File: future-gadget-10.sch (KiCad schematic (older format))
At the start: 38 parts, among them J1 Conn_02x05_Odd_Even, U1 ProMicro

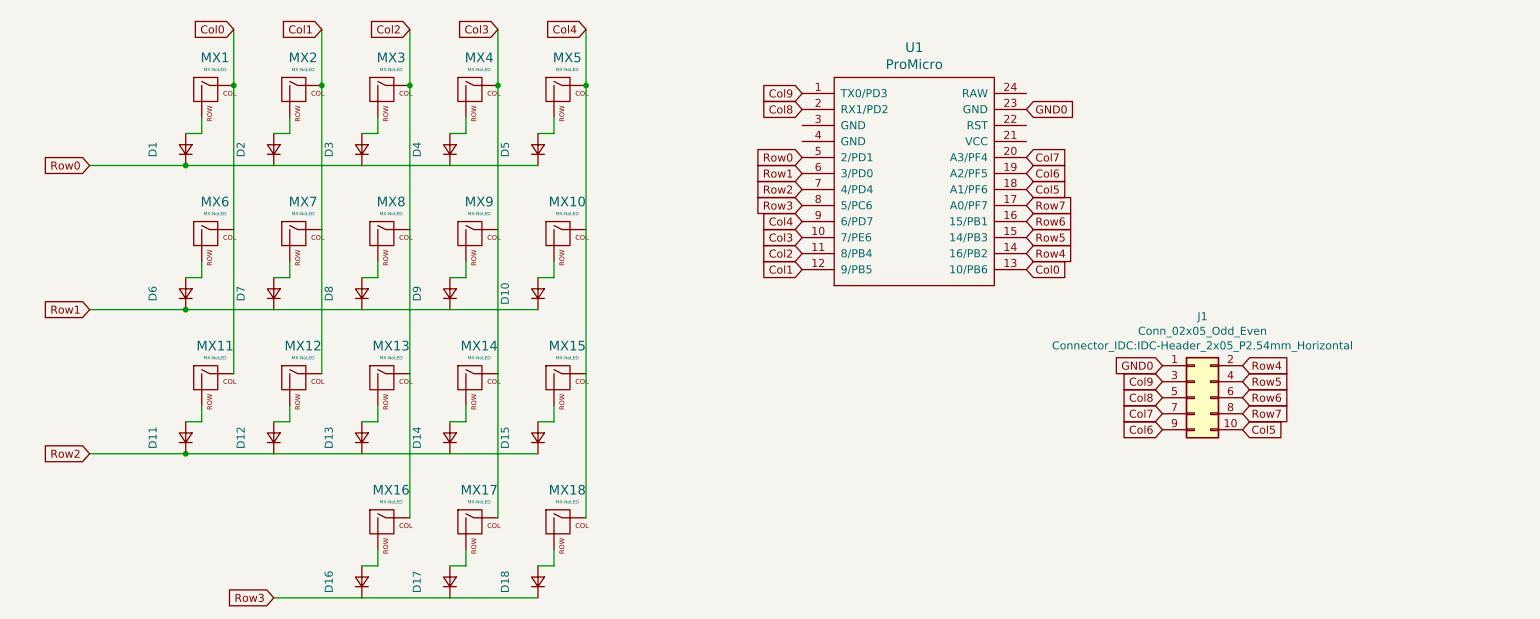
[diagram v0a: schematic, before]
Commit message: Adds right hand, and updates the connector to be vertical to avoid orientation issues.
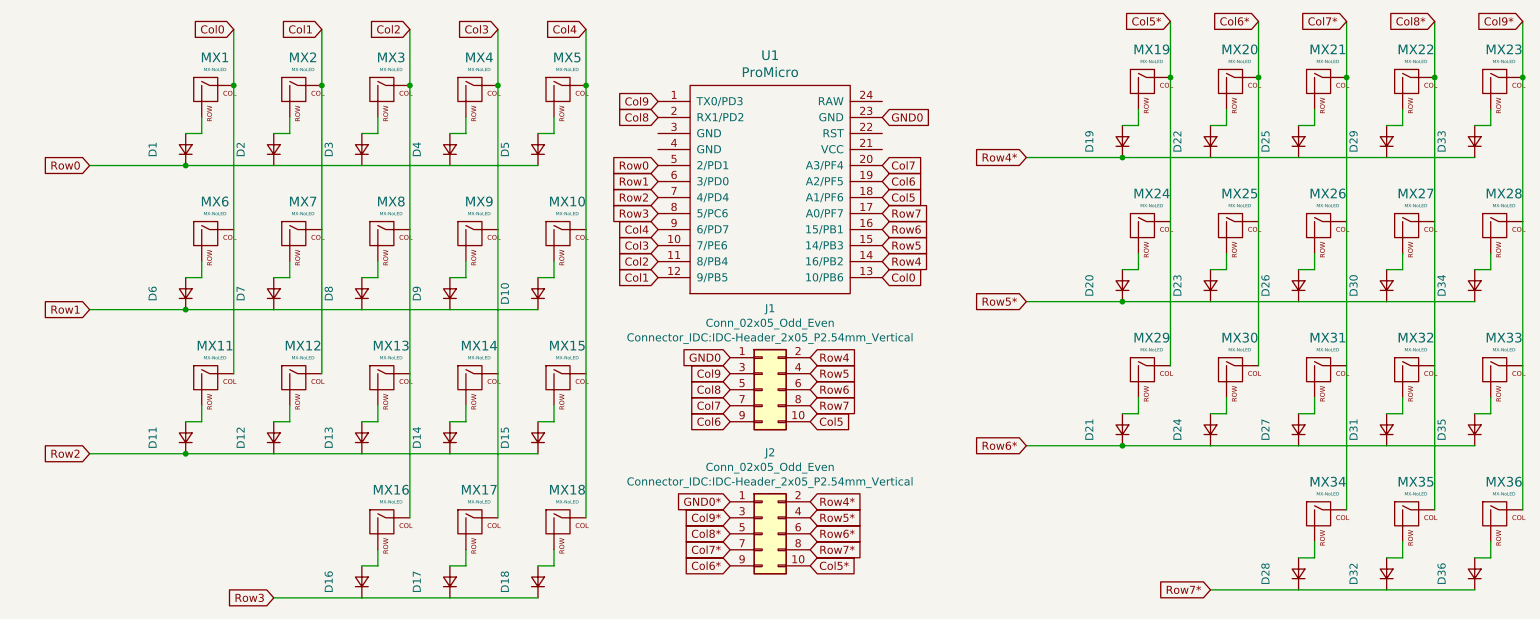
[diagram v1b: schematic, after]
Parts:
- added D19, D20, D21, D22, D23, D24, D25, D26, D27, D28, D29, D30, D31, D32, D33, D34, D35, D36: D_Small, Diode_SMD:D_SOD-123, symbol Device:D_Small
- added J2: Conn_02x05_Odd_Even, Connector_IDC:IDC-Header_2x05_P2.54mm_Vertical, symbol Connector_Generic:Conn_02x05_Odd_Even
- added MX19, MX20, MX21, MX22, MX23, MX24, MX25, MX26, MX27, MX28, MX29, MX30, MX31, MX32, MX33, MX34, MX35, MX36: MX-NoLED, MX_Only:MXOnly-1U-Hotswap, symbol MX_Alps_Hybrid:MX-NoLED
- J1: footprint Connector_IDC:IDC-Header_2x05_P2.54mm_Horizontal -> Connector_IDC:IDC-Header_2x05_P2.54mm_Vertical
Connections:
- new net: D19.2 (A), MX19.2 (ROW)
- new net: D22.2 (A), MX20.2 (ROW)
- new net: D23.2 (A), MX25.2 (ROW)
- new net: D20.2 (A), MX24.2 (ROW)
- new net: D25.2 (A), MX21.2 (ROW)
- new net: D26.2 (A), MX26.2 (ROW)
- new net: D29.2 (A), MX22.2 (ROW)
- new net: D30.2 (A), MX27.2 (ROW)
- new net: D33.2 (A), MX23.2 (ROW)
- new net: D34.2 (A), MX28.2 (ROW)
- new net: D24.2 (A), MX30.2 (ROW)
- new net: D21.2 (A), MX29.2 (ROW)
- new net: D27.2 (A), MX31.2 (ROW)
- new net: D31.2 (A), MX32.2 (ROW)
- new net: D35.2 (A), MX33.2 (ROW)
- new net: D28.2 (A), MX34.2 (ROW)
- new net: D32.2 (A), MX35.2 (ROW)
- new net: D36.2 (A), MX36.2 (ROW)
- new net Col5*: J2.10 (Pin_10), MX19.1 (COL), MX24.1 (COL), MX29.1 (COL)
- new net Col6*: J2.9 (Pin_9), MX20.1 (COL), MX25.1 (COL), MX30.1 (COL)
- new net Col7*: J2.7 (Pin_7), MX21.1 (COL), MX26.1 (COL), MX31.1 (COL), MX34.1 (COL)
- new net Col8*: J2.5 (Pin_5), MX22.1 (COL), MX27.1 (COL), MX32.1 (COL), MX35.1 (COL)
- new net Col9*: J2.3 (Pin_3), MX23.1 (COL), MX28.1 (COL), MX33.1 (COL), MX36.1 (COL)
- new net GND0*: J2.1 (Pin_1)
- new net Row4*: D19.1 (K), D22.1 (K), D25.1 (K), D29.1 (K), D33.1 (K), J2.2 (Pin_2)
- new net Row5*: D20.1 (K), D23.1 (K), D26.1 (K), D30.1 (K), D34.1 (K), J2.4 (Pin_4)
- new net Row6*: D21.1 (K), D24.1 (K), D27.1 (K), D31.1 (K), D35.1 (K), J2.6 (Pin_6)
- new net Row7*: D28.1 (K), D32.1 (K), D36.1 (K), J2.8 (Pin_8)
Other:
- moved on the sheet: J1, U1

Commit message: A little rerouting and a switch of footprints for the MX hotswaps so they render in 3D.
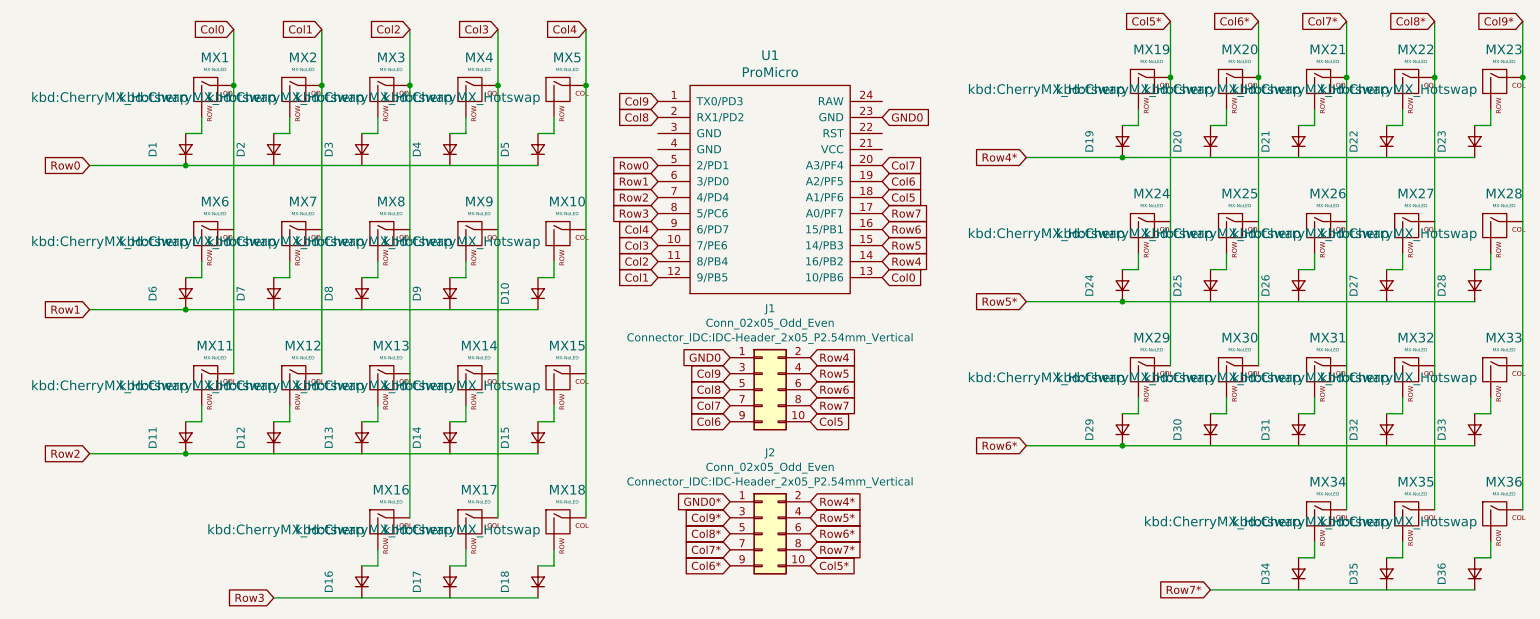
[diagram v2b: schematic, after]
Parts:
- MX1, MX10, MX11, MX12, MX13, MX14, MX15, MX16, MX17, MX18, MX19, MX2, MX20, MX21, MX22, MX23, MX24, MX25, MX26, MX27, MX28, MX29, MX3, MX30, MX31, MX32, MX33, MX34, MX35, MX36, MX4, MX5, MX6, MX7, MX8, MX9: footprint MX_Only:MXOnly-1U-Hotswap -> kbd:CherryMX_Hotswap
- renumbered D22 to D20, D25 to D21, D29 to D22, D33 to D23, D20 to D24, D23 to D25, D30 to D27, D34 to D28, D21 to D29, D24 to D30, D27 to D31, D31 to D32, D35 to D33, D28 to D34, D32 to D35
